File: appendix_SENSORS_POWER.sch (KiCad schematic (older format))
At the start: 50 parts, among them J401 Conn_01x02, J402 Conn_01x02, J403 Screw_Terminal_01x02, J404 Conn_01x02, J405 Conn_01x02, J406 Screw_Terminal_01x02, J407 Conn_01x02, J408 Conn_01x02, J409 Conn_01x02, J410 Conn_01x02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

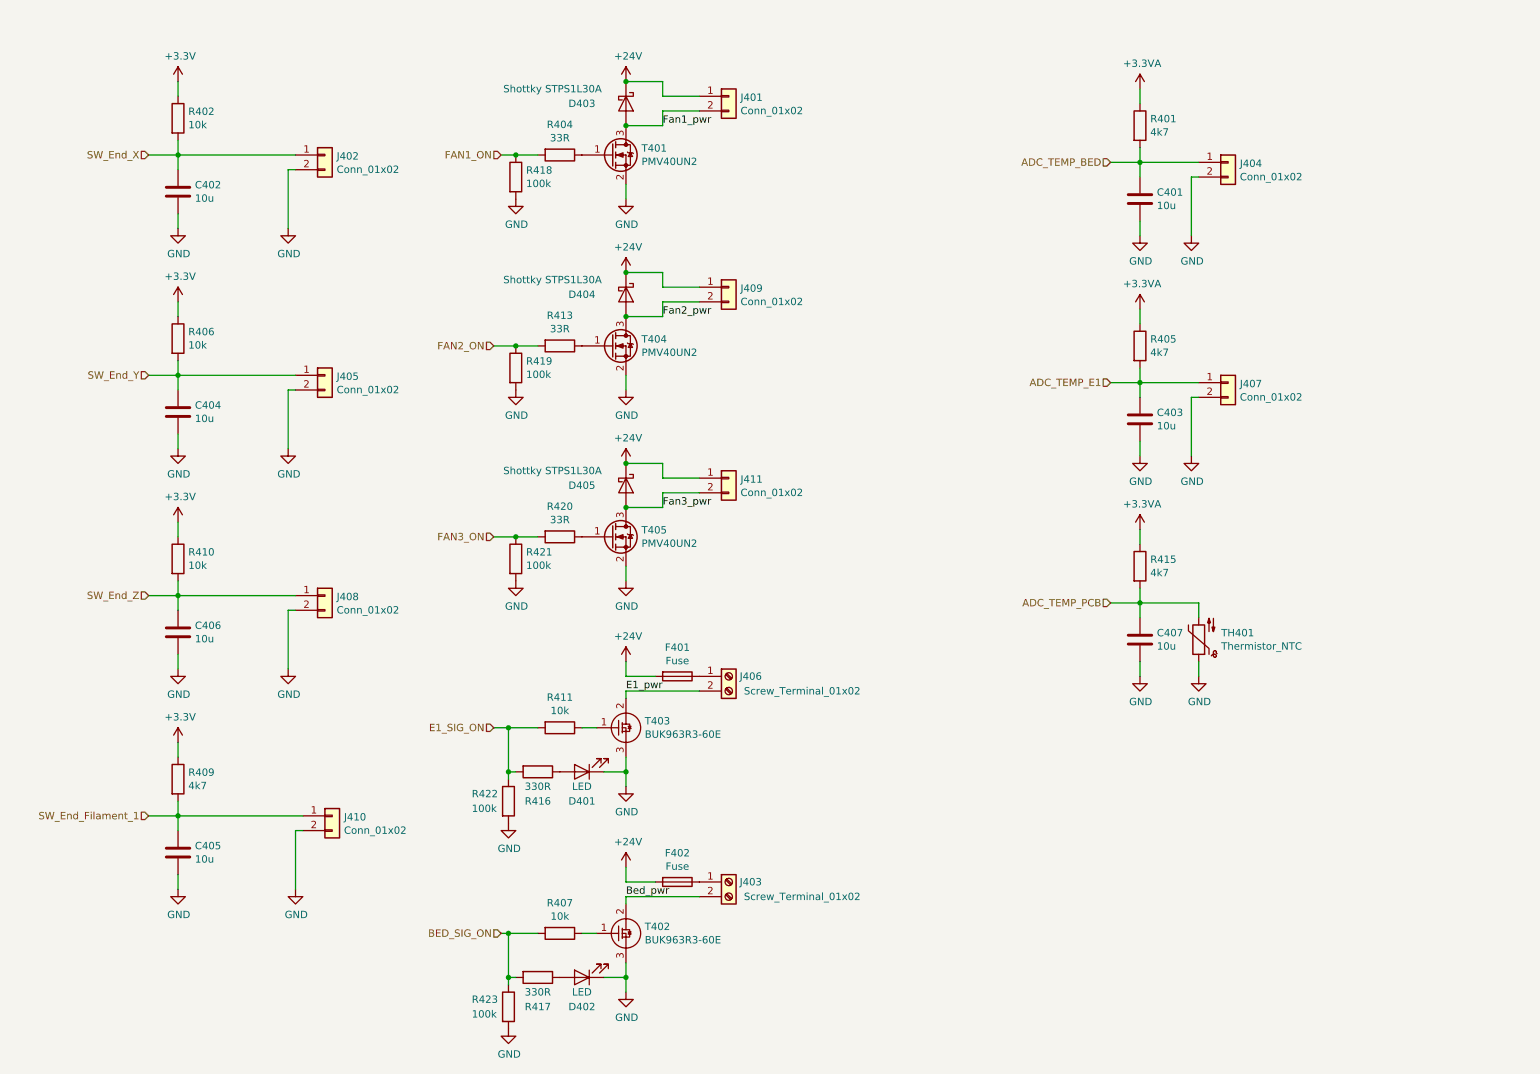
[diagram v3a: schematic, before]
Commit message: TVS protection, BOOT1 pin, user BTN
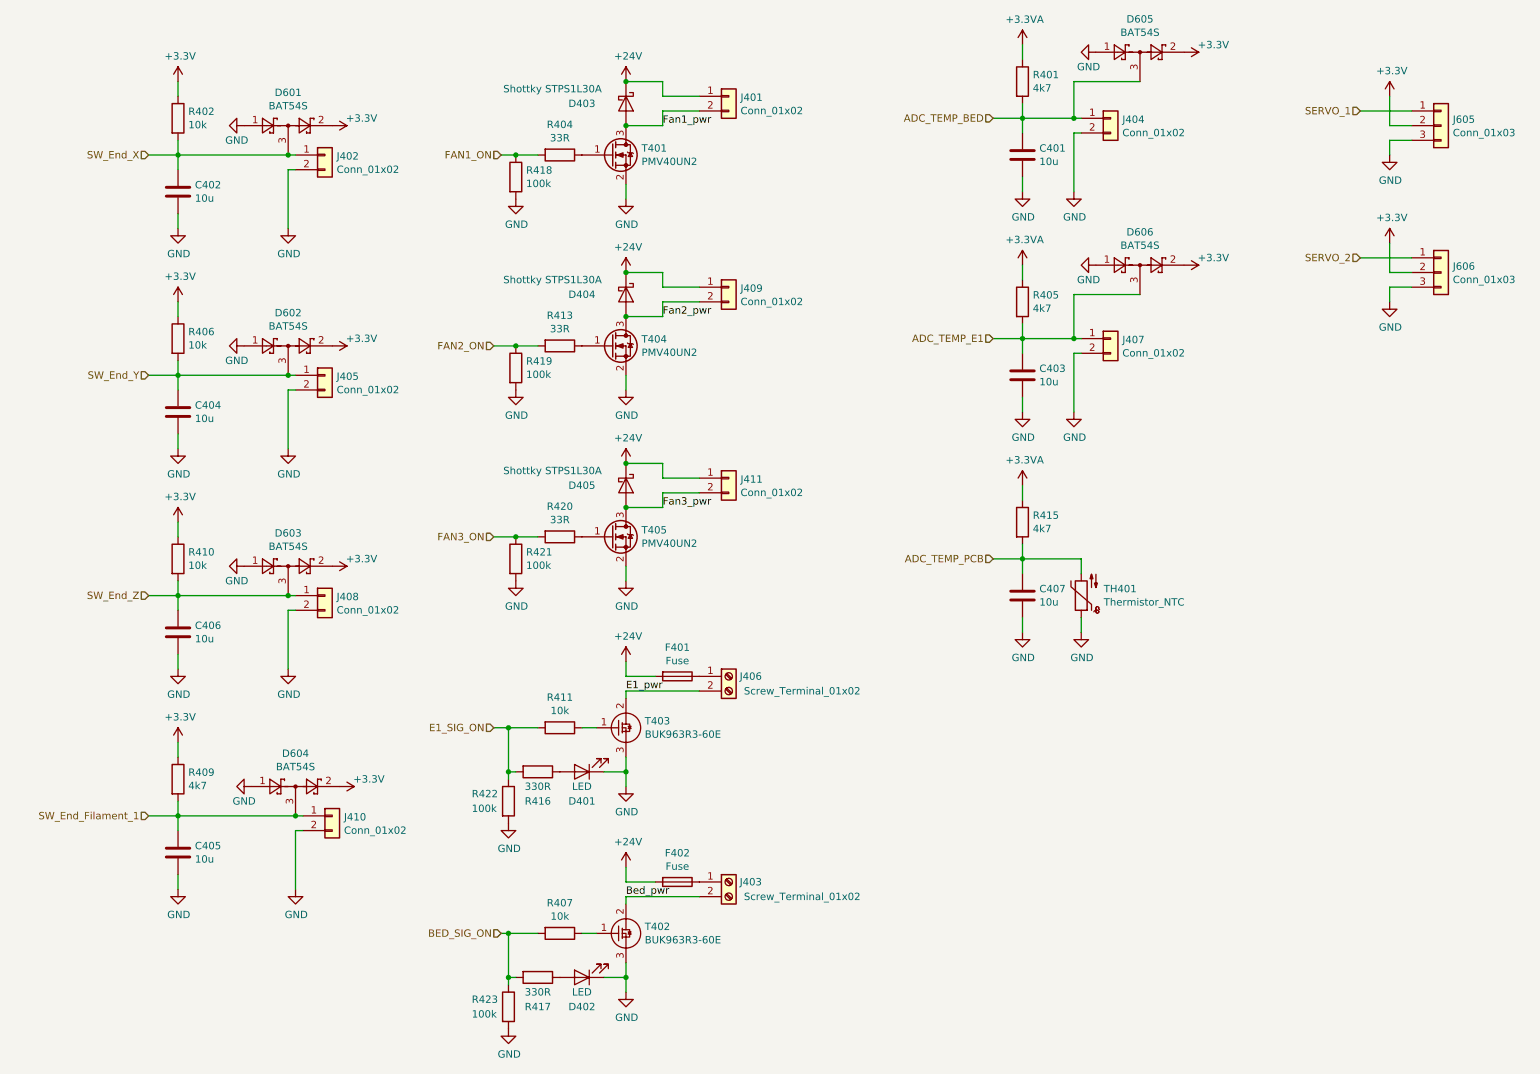
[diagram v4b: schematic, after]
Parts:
- added D601, D602, D603, D604, D605, D606: BAT54S, Package_TO_SOT_SMD:SOT-23, symbol Diode:BAT54S
- added J605, J606: Conn_01x03, Connector_PinHeader_2.54mm:PinHeader_1x03_P2.54mm_Vertical, symbol Connector_Generic:Conn_01x03
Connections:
- net +3V3: now also D601.2, D602.2, D603.2, D604.2, D605.2, D606.2, J605.2 (Pin_2), J606.2 (Pin_2)
- net ADC_TEMP_BED: now also D605.3
- net ADC_TEMP_E1: now also D606.3
- net GND: now also D601.1, D602.1, D603.1, D604.1, D605.1, D606.1, J605.3 (Pin_3), J606.3 (Pin_3)
- net SW_End_Filament_1: now also D604.3
- net SW_End_X: now also D601.3
- net SW_End_Y: now also D602.3
- net SW_End_Z: now also D603.3
- new net SERVO_1: J605.1 (Pin_1)
- new net SERVO_2: J606.1 (Pin_1)
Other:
- moved on the sheet: C401, C403, C407, J404, J407, R401, R405, R415, TH401

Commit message: finished up for final review
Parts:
- added D607, D608: BAT54S, Package_TO_SOT_SMD:SOT-23, symbol Diode:BAT54S
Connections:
- net +3V3: now also D607.2, D608.2
- net GND: now also D607.1, D608.1
- net SERVO_1: now also D607.3
- net SERVO_2: now also D608.3
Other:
- moved on the sheet: C401, C403, C407, D605, D606, J404, J407, J605, J606, R401, R405, R415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

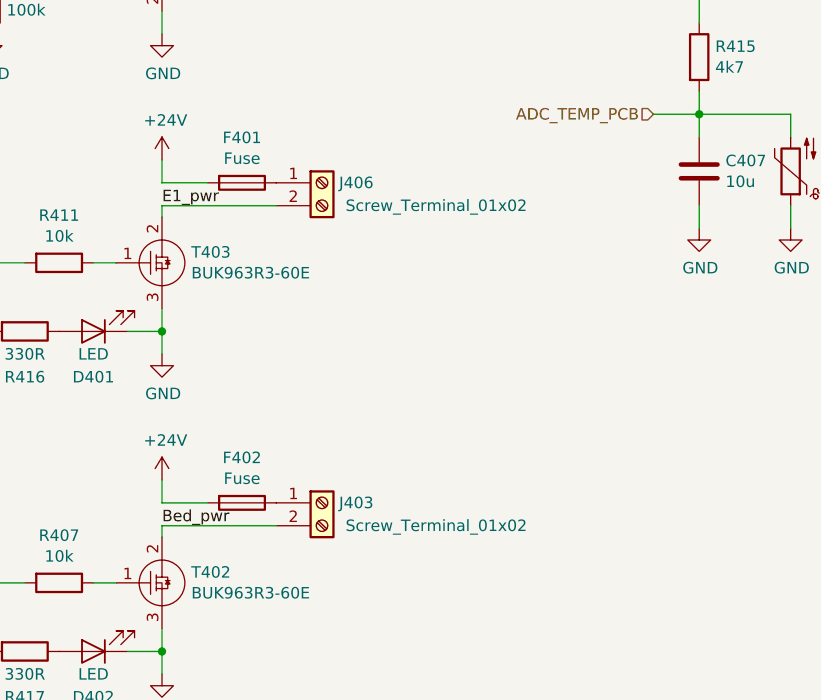
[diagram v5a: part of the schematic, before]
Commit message: changed screw terminal for bed/ext
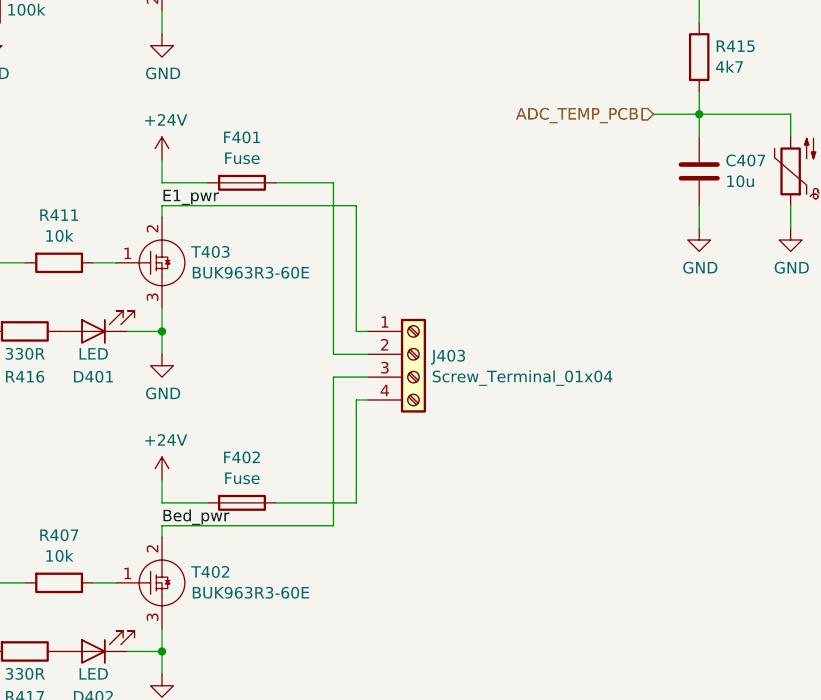
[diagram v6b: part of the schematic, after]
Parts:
- removed J403, J406: Screw_Terminal_01x02, Connectors_Terminal_Blocks:TerminalBlock_Altech_AK300-2_P5.00mm, symbol Connector:Screw_Terminal_01x02
- added J403: Screw_Terminal_01x04, Connectors_Terminal_Blocks:TerminalBlock_Altech_AK300-4_P5.00mm, symbol Connector:Screw_Terminal_01x04
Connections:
- net Bed_pwr: now also J403.3 (Pin_3)
- net E1_pwr: now also J403.1 (Pin_1)
- net at F401.1: now also J403.2 (Pin_2)
- net at F402.1: now also J403.4 (Pin_4)
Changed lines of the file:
@@
 	4750 6650 4750 6600
 Wire Wire Line
-	4750 6600 5250 6600
-Wire Wire Line
 	4750 6500 4750 6400
 $Comp
@@
 	4750 5250 4750 5200
 Wire Wire Line
-	4750 5200 5250 5200
-Wire Wire Line
 	7100 2200 7100 2300
 Wire Wire Line
@@
 $EndComp
 $Comp
-L Connector:Screw_Terminal_01x02 J?
-U 1 1 5CE15986
-P 5450 6500
-AR Path="/5CE15986" Ref="J?"  Part="1"
-AR Path="/5CA39F21/5CE15986" Ref="J403"  Part="1"
-F 0 "J403" H 5600 6500 50  0000 C CNN
-F 1 "Screw_Terminal_01x02" H 5950 6400 50  0000 C CNN
-F 2 "Connectors_Terminal_Blocks:TerminalBlock_Altech_AK300-2_P5.00mm" H 5450 6500 50  0001 C CNN
-F 3 "~" H 5450 6500 50  0001 C CNN
-	1    5450 6500
-	1    0    0    -1
-$EndComp
-$Comp
 L power:GND #PWR0406
 U 1 1 5CE79ADB
@@
 Wire Wire Line
 	7450 3400 7500 3400
-$Comp
-L Connector:Screw_Terminal_01x02 J?
-U 1 1 5CE79AE7
-P 5450 5100
-AR Path="/5CE79AE7" Ref="J?"  Part="1"
-AR Path="/5CA39F21/5CE79AE7" Ref="J406"  Part="1"
-F 0 "J406" H 5600 5100 50  0000 C CNN
-F 1 "Screw_Terminal_01x02" H 5950 5000 50  0000 C CNN
-F 2 "Connectors_Terminal_Blocks:TerminalBlock_Altech_AK300-2_P5.00mm" H 5450 5100 50  0001 C CNN
-F 3 "~" H 5450 5100 50  0001 C CNN
-	1    5450 5100
-	1    0    0    -1
-$EndComp
 Wire Wire Line
 	7100 3300 7450 3300
@@
 Wire Wire Line
 	9900 3000 9900 3400
+Wire Wire Line
+	4750 6600 5500 6600
+Wire Wire Line
+	5600 6500 5600 6050
+Wire Wire Line
+	5600 6050 5650 6050
+Wire Wire Line
+	5250 6500 5600 6500
+Wire Wire Line
+	5650 5950 5500 5950
+Wire Wire Line
+	5500 5950 5500 6600
+$Comp
+L Connector:Screw_Terminal_01x04 J403
+U 1 1 5CC229A7
+P 5850 5850
+F 0 "J403" H 5930 5842 50  0000 L CNN
+F 1 "Screw_Terminal_01x04" H 5930 5751 50  0000 L CNN
+F 2 "Connectors_Terminal_Blocks:TerminalBlock_Altech_AK300-4_P5.00mm" H 5850 5850 50  0001 C CNN
+F 3 "~" H 5850 5850 50  0001 C CNN
+	1    5850 5850
+	1    0    0    -1
+$EndComp
+Wire Wire Line
+	5250 5100 5500 5100
+Wire Wire Line
+	5500 5100 5500 5850
+Wire Wire Line
+	5500 5850 5650 5850
+Wire Wire Line
+	5650 5750 5600 5750
+Wire Wire Line
+	5600 5750 5600 5200
+Wire Wire Line
+	5600 5200 4750 5200
 $EndSCHEMATC

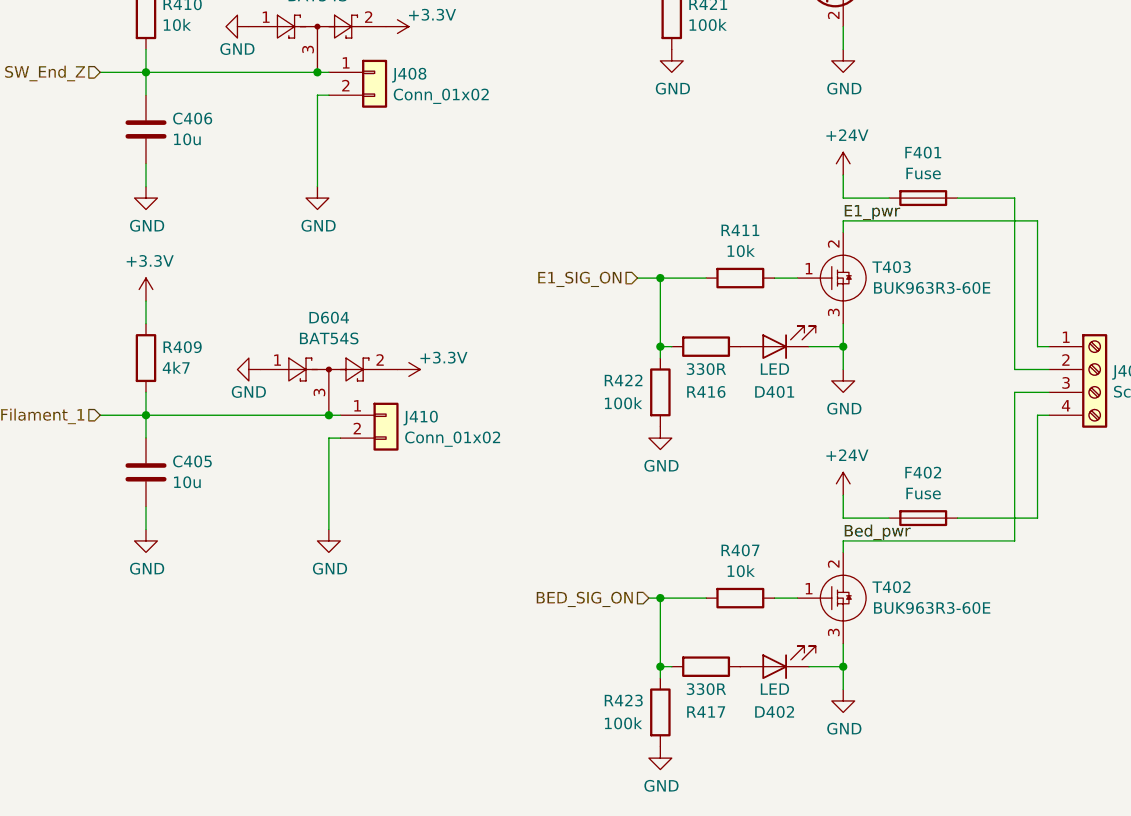
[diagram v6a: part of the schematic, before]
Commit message: added comments from comments branch corrected silk Servo2 added title to schematic pages
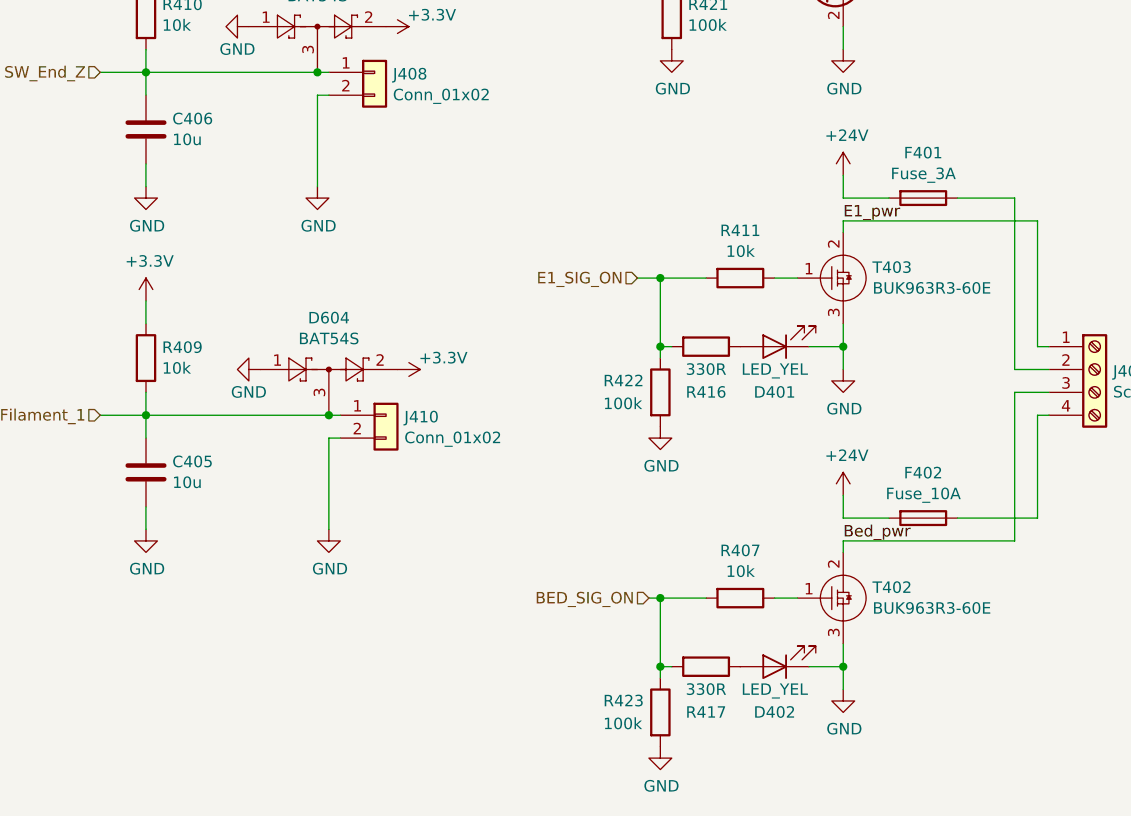
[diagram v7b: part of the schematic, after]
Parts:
- D401, D402: value LED -> LED_YEL
- F401: value Fuse -> Fuse_3A
- F402: value Fuse -> Fuse_10A
- R409: value 4k7 -> 10k
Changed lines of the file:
@@
 encoding utf-8
 Sheet 6 6
-Title ""
-Date ""
-Rev "1"
-Comp ""
+Title "Power and Sensor Connectors"
+Date "2019-05-10"
+Rev "1.1"
+Comp "FHNW University of Applied Sciences"
 Comment1 "EIT Pro4 FS19 Team 8"
 Comment2 ""
@@
 P 1700 5800
 F 0 "R409" H 1770 5846 50  0000 L CNN
-F 1 "4k7" H 1770 5755 50  0000 L CNN
+F 1 "10k" H 1770 5755 50  0000 L CNN
 F 2 "Resistors_SMD:R_0603" V 1630 5800 50  0001 C CNN
 F 3 "~" H 1700 5800 50  0001 C CNN
@@
 AR Path="/5CA39F21/5CB6EFDE" Ref="D401"  Part="1"
 F 0 "D401" H 4450 5950 50  0000 C CNN
-F 1 "LED" H 4450 5850 50  0000 C CNN
+F 1 "LED_YEL" H 4450 5850 50  0000 C CNN
 F 2 "LED_SMD:LED_0805_2012Metric" H 4450 5750 50  0001 C CNN
 F 3 "~" H 4450 5750 50  0001 C CNN
@@
 AR Path="/5CA39F21/5CBB2518" Ref="D402"  Part="1"
 F 0 "D402" H 4450 7350 50  0000 C CNN
-F 1 "LED" H 4450 7250 50  0000 C CNN
+F 1 "LED_YEL" H 4450 7250 50  0000 C CNN
 F 2 "LED_SMD:LED_0805_2012Metric" H 4450 7150 50  0001 C CNN
 F 3 "~" H 4450 7150 50  0001 C CNN
@@
 AR Path="/5CB755BC" Ref="F?"  Part="1"
 F 0 "F401" V 4903 5100 50  0000 C CNN
-F 1 "Fuse" V 4994 5100 50  0000 C CNN
+F 1 "Fuse_3A" V 4994 5100 50  0000 C CNN
 F 2 "Fuse:Fuseholder_Blade_ATO_Littelfuse_Pudenz_2_Pin" V 5030 5100 50  0001 C CNN
 F 3 "~" H 5100 5100 50  0001 C CNN
@@
 AR Path="/5CB7E081" Ref="F?"  Part="1"
 F 0 "F402" V 4903 6500 50  0000 C CNN
-F 1 "Fuse" V 4994 6500 50  0000 C CNN
+F 1 "Fuse_10A" V 4994 6500 50  0000 C CNN
 F 2 "Fuse:Fuseholder_Blade_ATO_Littelfuse_Pudenz_2_Pin" V 5030 6500 50  0001 C CNN
 F 3 "~" H 5100 6500 50  0001 C CNN

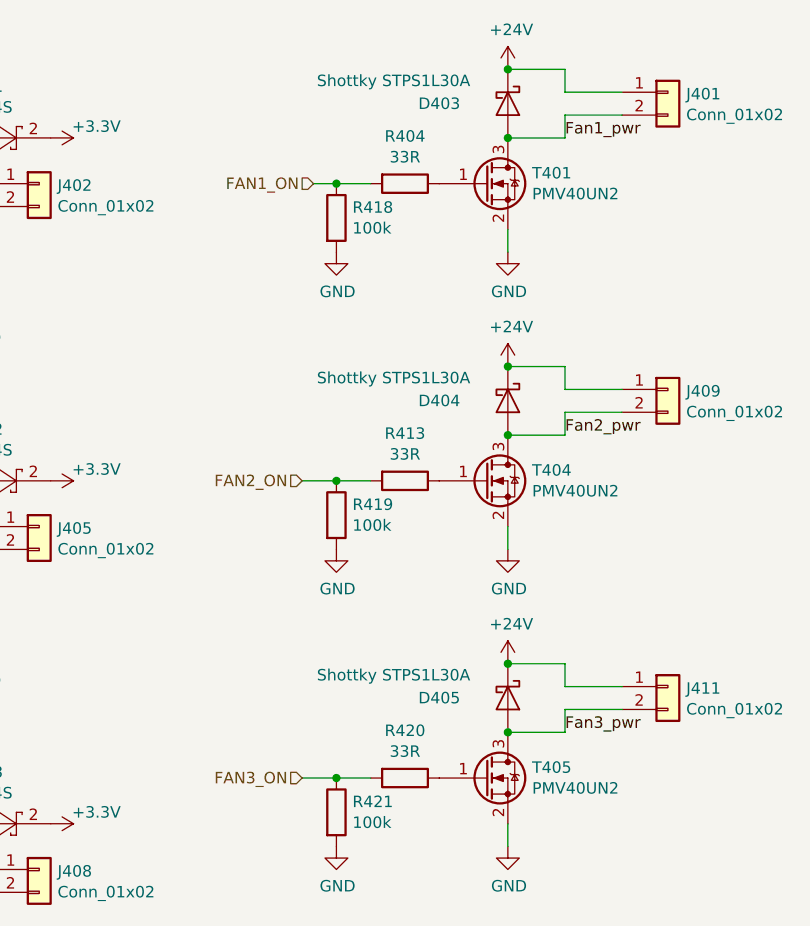
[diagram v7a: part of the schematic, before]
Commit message: clarified some component values and printed PDFs
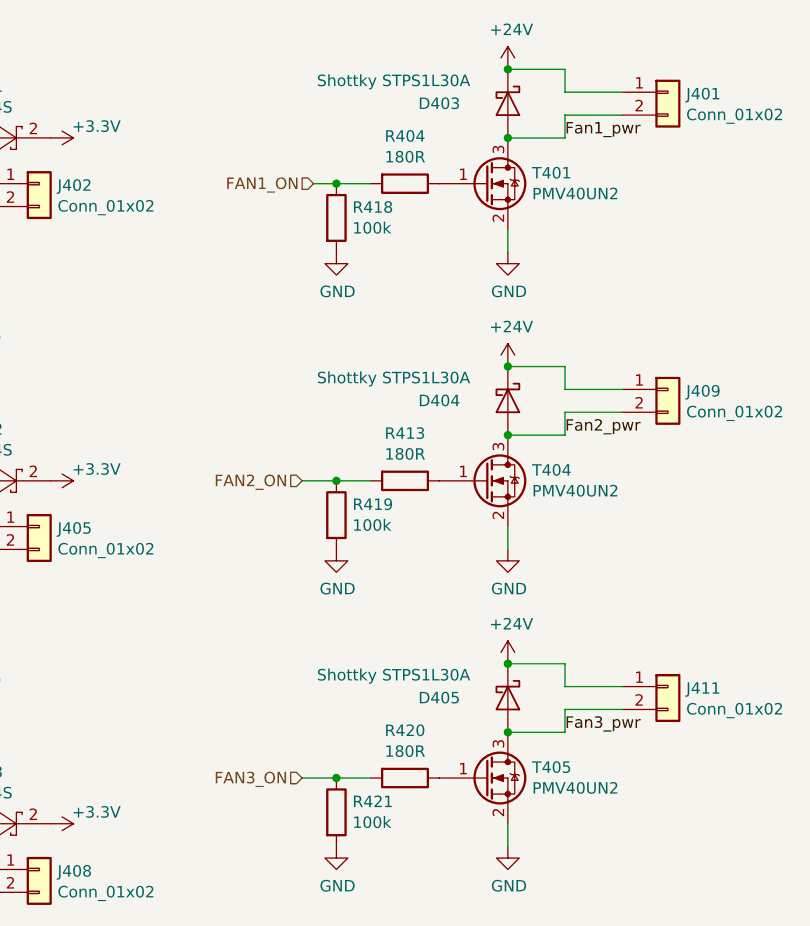
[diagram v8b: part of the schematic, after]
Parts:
- R404, R413, R420: value 33R -> 180R
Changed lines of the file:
@@
 P 4300 1550
 F 0 "R404" V 4093 1550 50  0000 C CNN
-F 1 "33R" V 4184 1550 50  0000 C CNN
+F 1 "180R" V 4184 1550 50  0000 C CNN
 F 2 "Resistors_SMD:R_0603" V 4230 1550 50  0001 C CNN
 F 3 "~" H 4300 1550 50  0001 C CNN
@@
 P 4300 2850
 F 0 "R413" V 4093 2850 50  0000 C CNN
-F 1 "33R" V 4184 2850 50  0000 C CNN
+F 1 "180R" V 4184 2850 50  0000 C CNN
 F 2 "Resistors_SMD:R_0603" V 4230 2850 50  0001 C CNN
 F 3 "~" H 4300 2850 50  0001 C CNN
@@
 P 4300 4150
 F 0 "R420" V 4093 4150 50  0000 C CNN
-F 1 "33R" V 4184 4150 50  0000 C CNN
+F 1 "180R" V 4184 4150 50  0000 C CNN
 F 2 "Resistors_SMD:R_0603" V 4230 4150 50  0001 C CNN
 F 3 "~" H 4300 4150 50  0001 C CNN
